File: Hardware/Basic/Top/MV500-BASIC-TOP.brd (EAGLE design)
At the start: 38 x 38 mm, 19 parts, among them U2 NRF52832_MODULE_MDBT42

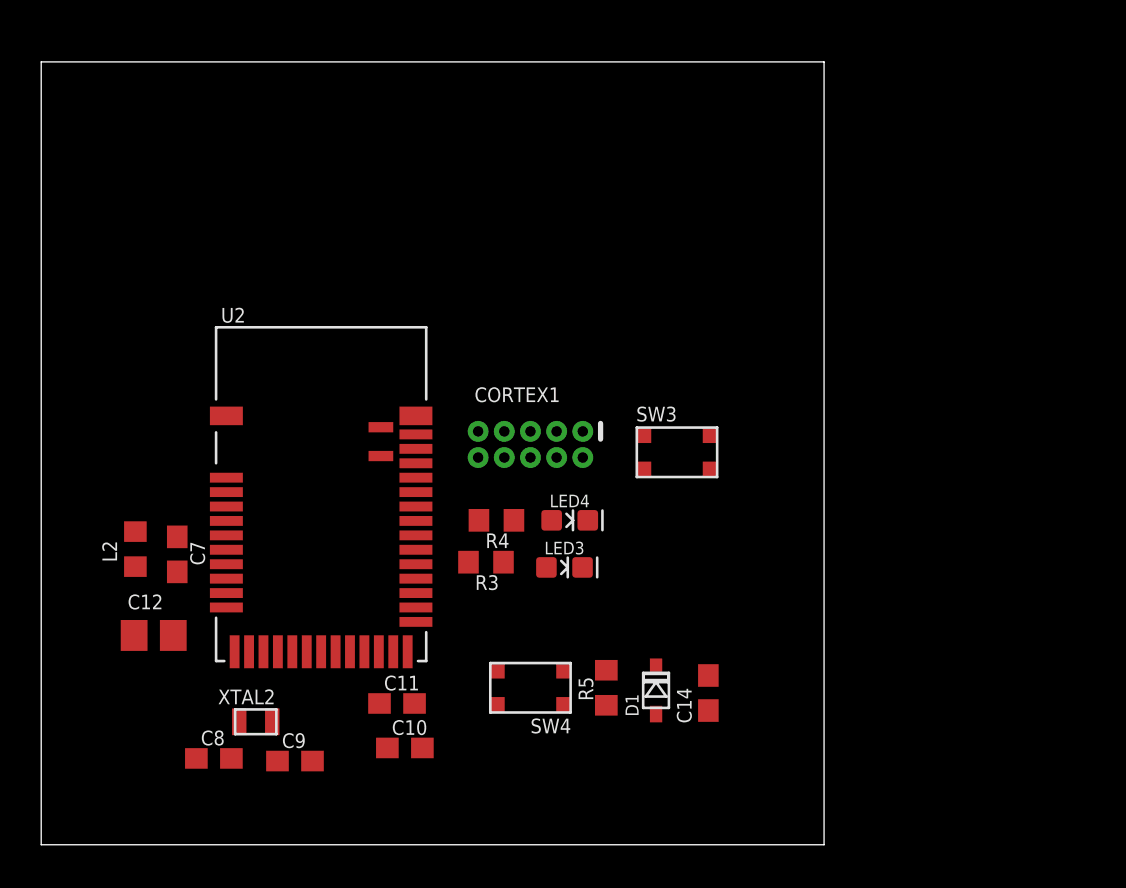
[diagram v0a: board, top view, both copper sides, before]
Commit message: Added OLED and SD Card
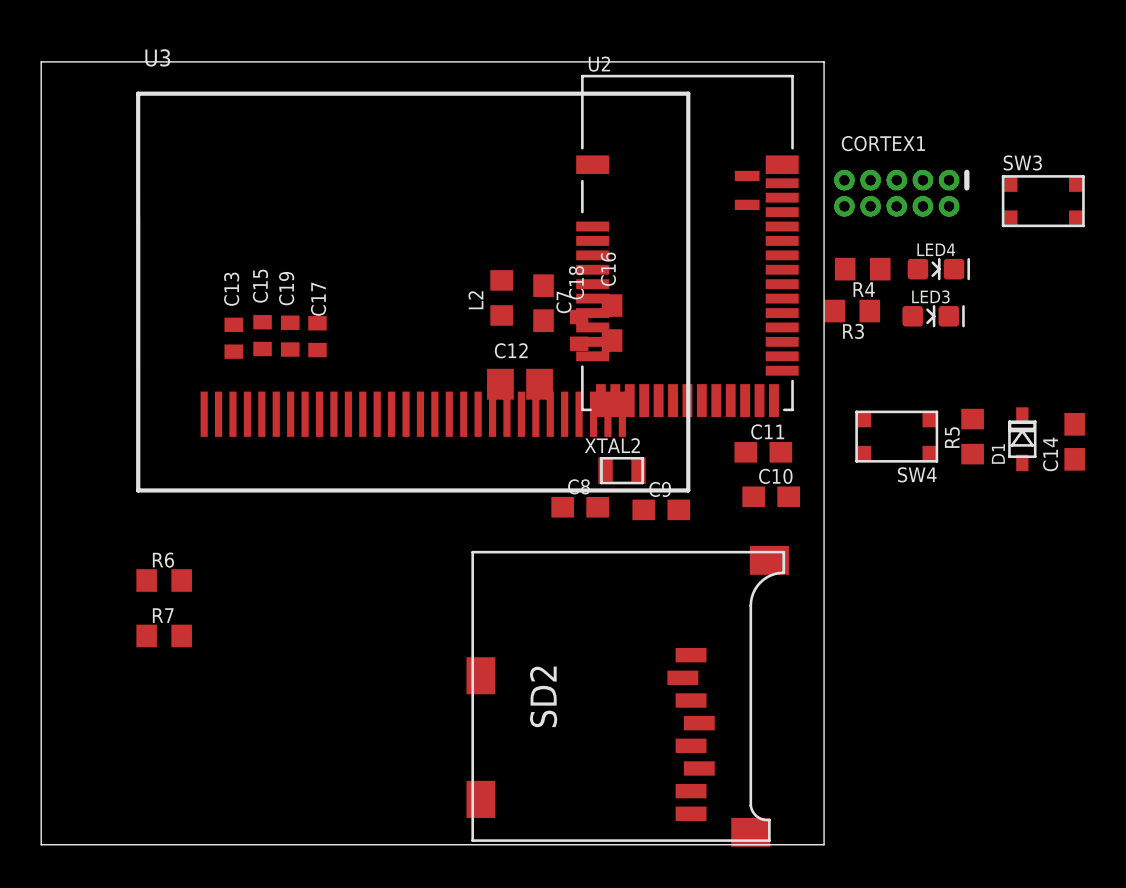
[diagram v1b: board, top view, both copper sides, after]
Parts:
- added C13, C15, C17, C18, C19: 2.2uF, LinnesLab-Passives:C0402
- added C16: 10uF, LinnesLab-Passives:C0603
- added R6: 10k, LinnesLab-Passives:R0603
- added R7: 390k, LinnesLab-Passives:R0603
- added SD2: (no value), LinnesLab-Connectors:MICROSD
- added U3: (no value), LinnesLab-Displays:UG-2864HSWEG01_0.96IN_NO-WRAPAROUND
- moved C10 21.6 mm to (35.4, 16.9)
- moved C11 21.6 mm to (35.1, 19.1)
- moved C12 21.6 mm to (23.2, 22.4)
- moved C14 21.6 mm to (50.2, 19.6)
- moved C7 21.6 mm to (24.4, 26.3)
- moved C8 21.6 mm to (26.2, 16.4)
- moved C9 21.6 mm to (30.1, 16.3)
- moved CORTEX1 21.6 mm to (41.5, 31.6)
- moved D1 21.6 mm to (47.6, 19.7)
- moved L2 21.6 mm to (22.4, 26.5)
- moved LED3 21.6 mm to (43.2, 25.7)
- moved R4 21.6 mm to (39.9, 27.9)
- moved R5 21.6 mm to (45.2, 19.8)
- moved SW4 21.6 mm to (41.5, 19.8)
- moved U2 21.6 mm to (31.4, 29.2)
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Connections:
- new net CD1: SD2.CD1
- new net CD2: SD2.CD2
- new net CS.OLED: U3.13
- new net DC.OLED: U3.15
- new net N$1: R6.2, U3.11
- new net N$13: C16.2, U3.28
- new net N$15: C18.2, U3.27
- new net N$2: R7.1, U3.26
- new net N$3: C13.2, U3.2
- new net N$5: C13.1, U3.3
- new net N$7: C15.2, U3.4
- new net N$8: C15.1, U3.5
- new net RESET.OLED: U3.14
- new net SD.CS: SD2.2
- net 3.3V: now also C17.2, C19.2, SD2.4, U3.6, U3.9
- net GND: now also C16.1, C17.1, C18.1, C19.1, R6.1, R7.2, SD2.6, SD2.MT1, SD2.MT2, U3.1, U3.10, U3.12, U3.29, U3.30, U3.8
- net MISO: now also SD2.7
- net MOSI: now also SD2.3, U3.19
- net SCK: now also SD2.5, U3.18

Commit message: Updated TOP Board
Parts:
- added C2, C5, C6: 1u, LinnesLab-Passives:C0603
- added C20, C21: 4.7u, LinnesLab-Passives:C0603
- added CHRG2: MCP73831, LinnesLab-Power:SOT23-5
- added D4, D5: (no value), LinnesLab-DiscreteSemi:USC
- added J2: (no value), LinnesLab-Connectors:1X02
- added LDO2: MIC5504, LinnesLab-Power:SOT23-5
- added R11: (no value), LinnesLab-Passives:R0603
- added R12, R13, R14, R15: 100k, LinnesLab-Passives:R0603
- added R8, R9: 10k, LinnesLab-Passives:R0603
- added SW1, SW2: SWITCH.MOM, LinnesLab-Switches:TACTILE_SWITCH_SMD_6.2MM_TALL
- added U4: PCF8523, LinnesLab-Clocks:SO8
- added USB2: USB.MICRO-BIGGERPADS, LinnesLab-Connectors:USB-MICRO-01.BIGGERPADS
- added XTAL3: 32.7680kHz, LinnesLab-Clocks:2-SMD.NOLEAD.2.0MMTO1.2MM
- moved SD2 24.3 mm to (20.9, 24.5), flipped to the bottom, turned to 269.1 degrees
- moved R7 12.0 mm to (6.22, 22.1)
- moved C10 10.0 mm to (34.5, 26.8)
- moved C14 10.0 mm to (49.2, 29.5)
- moved C16 10.0 mm to (26.7, 35.3)
- moved C19 10.0 mm to (11.1, 34.6)
- moved C7 10.0 mm to (23.4, 36.2)
- moved C8 10.0 mm to (25.2, 26.3)
- moved C9 10.0 mm to (29.1, 26.2)
- moved D1 10.0 mm to (46.7, 29.6)
- moved L2 10.0 mm to (21.4, 36.5)
- moved R3 10.0 mm to (38.4, 35.9)
- moved U2 10.0 mm to (30.4, 39.2)
- moved C11 10.0 mm to (34.1, 29.0)
- moved C12 10.0 mm to (22.3, 32.3)
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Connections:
- new net BATT: R13.1, R14.2
- new net CHRG.STAT: CHRG2.1, R12.1
- new net N$16: SW1.B1, SW1.B2
- new net N$17: CHRG2.5, R11.2
- new net N$18: SW2.B1, SW2.B2
- new net N$19: U4.2, XTAL3.P$1
- new net N$20: U4.1, XTAL3.P$2
- new net SW1: SW1.A1, SW2.A1
- new net USB+: USB2.3
- new net USB-: USB2.2
- new net VBATT: U4.3
- new net VIN: C21.2, C5.2, CHRG2.4, D4.-, D5.-, LDO2.1, LDO2.3, R12.2
- new net VLIPO: C20.1, CHRG2.3, D4.+, J2.2, R13.2
- new net V_USB: D5.+, USB2.1
- net 3.3V: now also C2.1, C6.1, LDO2.5, R15.2, R8.2, R9.2, U4.8
- net GND: now also C2.2, C20.2, C21.1, C5.1, C6.2, CHRG2.2, J2.1, LDO2.2, R11.1, R14.1, R15.1, U4.4, USB2.5, USB2.S1, USB2.S2, USB2.S3, USB2.S4, USB2.S5, USB2.S6
- net SCL: now also R8.1, U4.6
- net SDA: now also R9.1, U4.5

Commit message: Top Board Updated
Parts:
- added C22: 100n, LinnesLab-Passives:C0603
- added C23, C24: 47p, LinnesLab-Passives:C0603
- added JP2: (no value), LinnesLab-Switches:SMT-JUMPER_2_NO_SILK
- added LED5: RED, LinnesLab-LED:LED-0603
- added LED6: YELLOW, LinnesLab-LED:LED-0603
- added R1, R2: 0, LinnesLab-Passives:R0603
- added R17, R18: 27, LinnesLab-Passives:R0603
- added R19, R20: 1k, LinnesLab-Passives:R0603
- added U5: FT231XS, LinnesLab-DigitalIC:SSOP20_L
- R8, R9: value 10k -> 10K
- moved R9 40.5 mm to (-7.72, -1.73), turned to 0 degrees
- moved R8 38.2 mm to (-7.72, 0.97), turned to 0 degrees
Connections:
- net VBATT renamed VBAT
- removed net RXD: U2.21
- removed net TXD: U2.19
- new net !CTS: JP2.2, U5.9
- new net FT3V3: U5.13
- new net N$25: R17.2, U5.12
- new net N$26: R18.2, U5.11
- new net N$27: LED5.C, R19.2
- new net N$28: LED6.C, R20.2
- new net RXD_FT: R2.1, U5.4
- new net RXD_NRF: R1.2, U2.21
- new net RXLED: R19.1, U5.17
- new net TXD_FT: R1.1, U5.20
- new net TXD_NRF: R2.2, U2.19
- new net TXLED: R20.1, U5.10
- net 3.3V: now also C22.2, LED5.A, LED6.A, R8.1, R9.1, U5.14, U5.3; no longer R8.2, R9.2
- net DTR: now also U5.1
- net GND: now also C22.1, C23.2, C24.1, JP2.1, U5.16, U5.6
- net SCL: now also R9.2; no longer R8.1
- net SDA: now also R8.2; no longer R9.1
- net USB+: now also C23.1, R18.1
- net USB-: now also C24.2, R17.1
- net V_USB: now also U5.15

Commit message: Top Board
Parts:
- moved C14 45.2 mm to (4.14, 25.8)
- moved JP2 45.2 mm to (16.2, 36.2)
- moved LED5 45.2 mm to (33.7, 44.7)
- moved LED6 45.2 mm to (33.7, 40.9)
- moved R17 45.2 mm to (16.4, 42.8)
- moved R19 45.2 mm to (33.7, 37.1)
- moved R20 45.2 mm to (33.7, 33.3)
- moved SW3 45.2 mm to (2.62, 37.5)
- moved C22 45.2 mm to (29.9, 45.0)
- moved C23 45.2 mm to (29.9, 39.9)
- moved C24 45.2 mm to (29.9, 34.8)
- moved D1 45.2 mm to (1.60, 26.0)
- moved R18 45.2 mm to (17.1, 39.6)
- moved R9 41.9 mm to (0.74, 39.3)
- moved R8 41.9 mm to (0.74, 42.0)
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
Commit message: Updated Top Board
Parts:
- moved U2 25.2 mm to (29.0, 29.8)
- moved CHRG2 24.9 mm to (19.8, 19.0)
- moved SW4 14.9 mm to (14.3, 9.22)
- moved R3 12.3 mm to (48.5, 28.9)
- moved U3 12.3 mm to (20.1, 20.2)
- moved CORTEX1 11.4 mm to (41.7, 30.1)
- moved LED3 11.3 mm to (51.6, 29.3)
- moved R4 11.3 mm to (48.3, 31.6)
- moved LED4 11.3 mm to (51.8, 31.6)
- moved SD2 9.94 mm to (20.8, 14.6)
- moved C16 9.91 mm to (27.4, 25.4)
- moved C22 9.91 mm to (30.9, 35.1)
- moved JP2 9.91 mm to (17.2, 26.3)
- moved L2 9.91 mm to (22.1, 26.6)
- moved LED6 9.91 mm to (34.7, 31.1)
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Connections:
- removed net BATT: R13.1, R14.2
- removed net CD1: SD2.CD1
- removed net CHRG.STAT: CHRG2.1, R12.1
- removed net CS.OLED: U3.13
- removed net DC.OLED: U3.15
- removed net RESET.OLED: U3.14
- removed net SD.CS: SD2.2
- removed net SW1: SW1.A1, SW2.A1
- new net A4/BATT: R13.1, R14.2, U2.5
- new net A6/TIA: U2.7
- new net A7/PPG: U2.8
- new net D11/SW1: SW1.A1, U2.25
- new net D15/SW2: SW2.A1, U2.29
- new net D16/CS.OLED: U2.30, U3.13
- new net D27/CHRG.STATUS: CHRG2.1, R12.1, U2.4
- new net D29/LED.CTRL: U2.6
- new net D3/RESET.OLED: U2.16, U3.14
- new net D4/DC.OLED: U2.17, U3.15
- new net D5/CD1: SD2.CD1, U2.18
- new net D7/SD.CS: SD2.2, U2.20
